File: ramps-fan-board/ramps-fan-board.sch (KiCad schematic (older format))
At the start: 21 parts, among them J1 Screw_Terminal_01x02, J10 Screw_Terminal_01x02, J11 Screw_Terminal_01x02, J12 Screw_Terminal_01x02, J2 Conn_01x03, J3 Conn_02x04_Top_Bottom, J4 Conn_01x04, J5 Conn_02x04_Top_Bottom, J6 Conn_01x03, J7 Screw_Terminal_01x02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

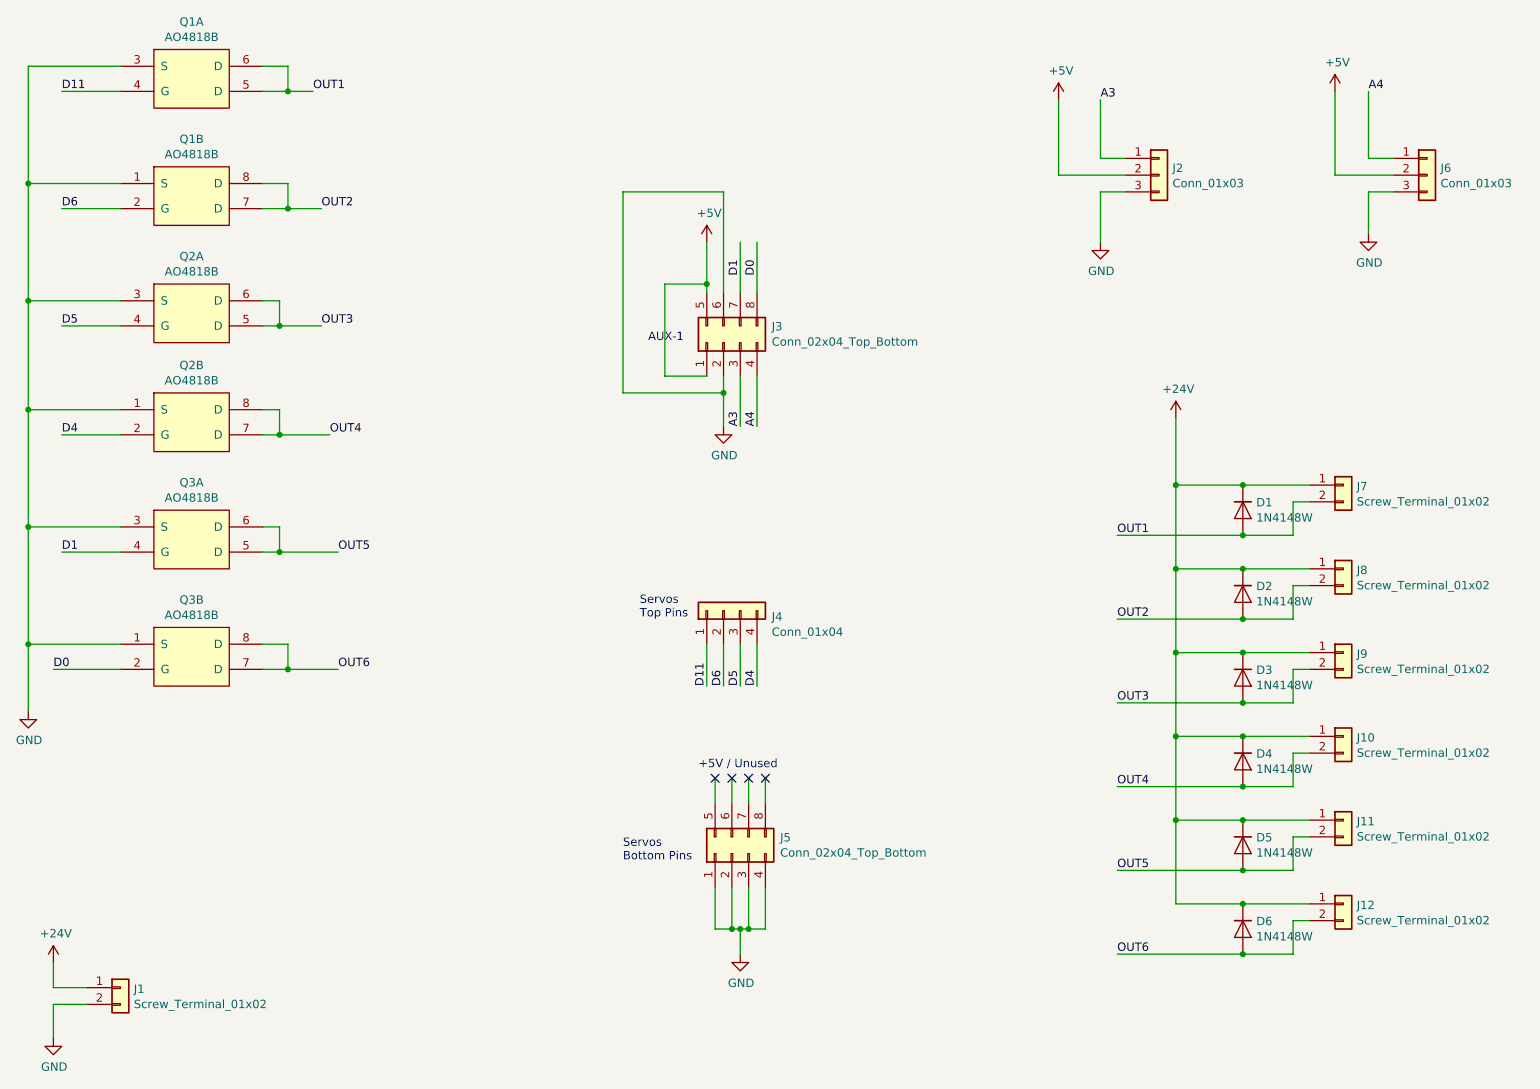
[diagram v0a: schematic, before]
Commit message: v1.5 (untested)
Still waiting on the v1.0 PCB's back for testing, but updated things
anyways.

- Add dedicated RGB 4 pin header
- Add Power plane on top of board
- Move SERVOS and AUX-1 parts to the back of the board
    - Updated pin outs to correspond to flipping the parts
- Improved silkscreening
- Add 2.5mm standoff hole
- Rename files to match the repo name
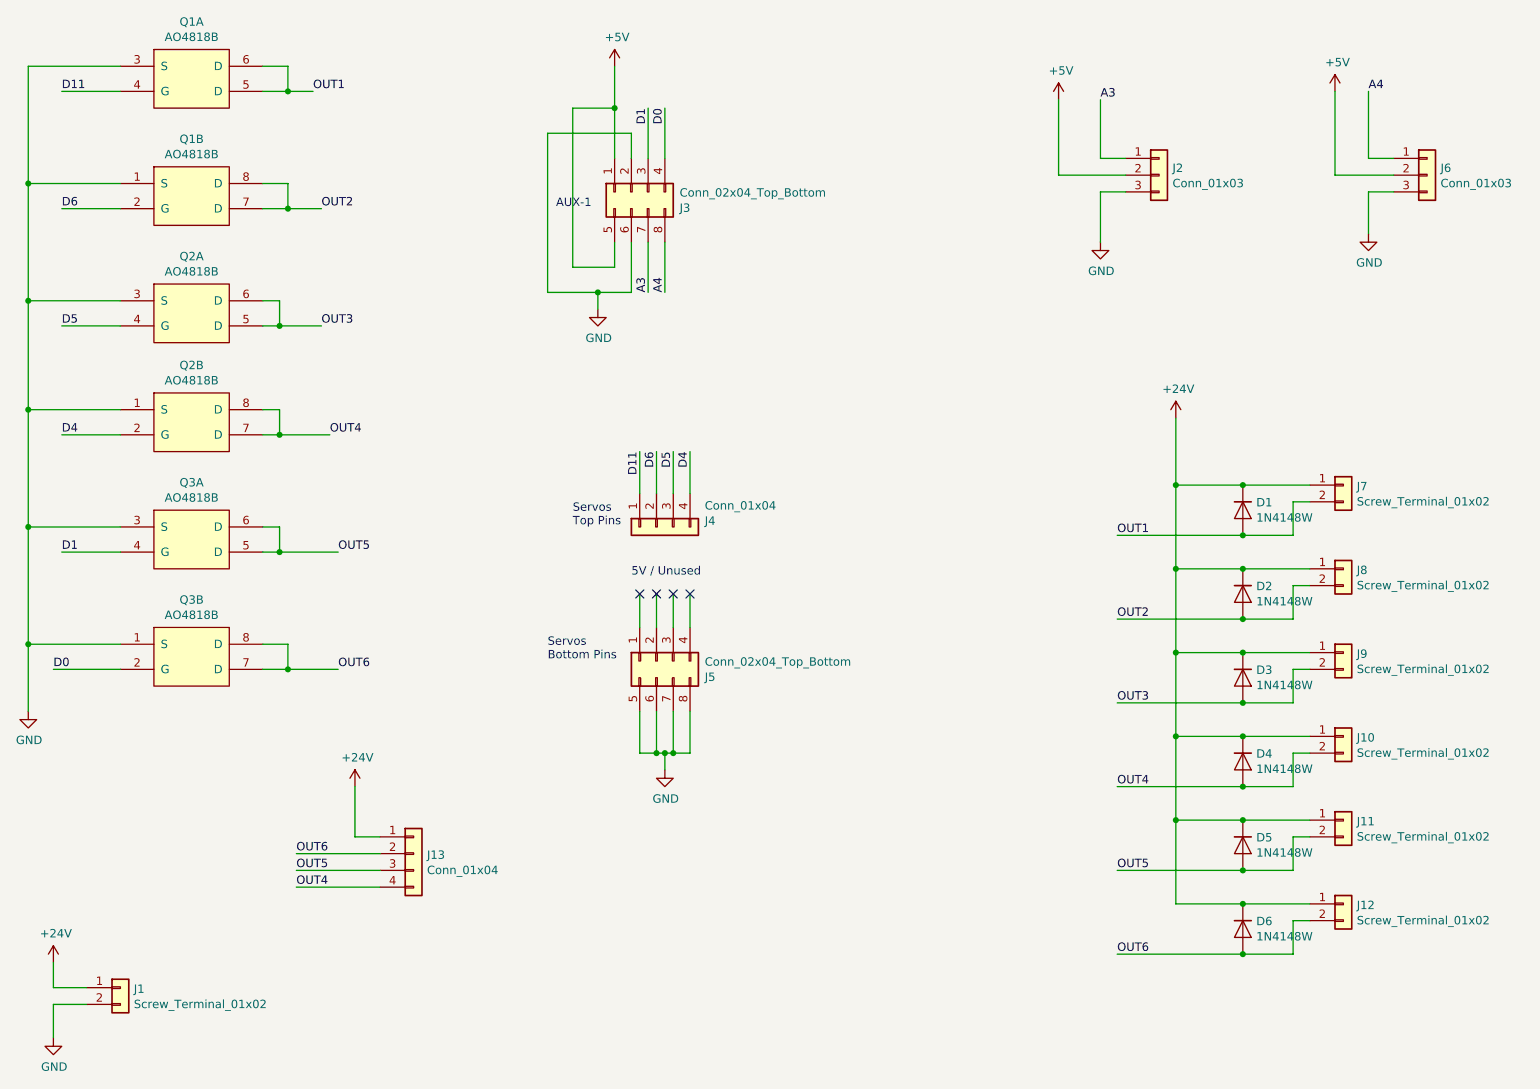
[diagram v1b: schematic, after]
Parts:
- added J13: Conn_01x04, Connector_Molex:Molex_KK-254_AE-6410-04A_1x04_P2.54mm_Vertical, symbol Connector_Generic:Conn_01x04
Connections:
- net +24V: now also J13.1 (Pin_1)
- net A3: now also J3.7 (Pin_7); no longer J3.3 (Pin_3)
- net A4: now also J3.8 (Pin_8); no longer J3.4 (Pin_4)
- net D0: now also J3.4 (Pin_4); no longer J3.8 (Pin_8)
- net D1: now also J3.3 (Pin_3); no longer J3.7 (Pin_7)
- net GND: now also J5.5 (Pin_5), J5.6 (Pin_6), J5.7 (Pin_7), J5.8 (Pin_8); no longer J5.1 (Pin_1), J5.2 (Pin_2), J5.3 (Pin_3), J5.4 (Pin_4)
- net OUT4: now also J13.4 (Pin_4)
- net OUT5: now also J13.3 (Pin_3)
- net OUT6: now also J13.2 (Pin_2)
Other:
- note added: "5V / Unused"
- note removed: "+5V / Unused\n"
- moved on the sheet: J3, J4, J5
